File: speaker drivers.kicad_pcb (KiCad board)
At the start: 2 copper layers, 82 x 36.9 mm, 43 parts, among them CN2 10uFE, CN3 0.1uFC

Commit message: WIP: Preliminary commit before splitting boards
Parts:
- removed CG2: 10uFE, LBHB:capacitor-D_4mm-L_2.4mm
- removed Cvr1: 0.33uF, LBHB:capacitor-2.5x5mm-L_2.5mm
- removed Cvr2: 0.1uF, LBHB:capacitor-2.5x5mm-L_2.5mm
- removed RS1: 100k, LBHB:resistor-6x2.3mm
- removed SER1: 8P_miniDIN, LBHB:mini-DIN-8-pin
- removed SIGIN1, SIGOUT1: 4P_miniDIN, LBHB:mini-DIN-4-pin
- removed VCTL1: PGA2310, LBHB:DIP-16
- removed VREG1: 78L05, LBHB:TO-92-bent
- added BNCLin1: BNC, Socket_Strips:Socket_Strip_Straight_1x02, F.Cu at (96.2, 92.6)
- added BNCRin1: BNC, Socket_Strips:Socket_Strip_Straight_1x02, F.Cu at (96.2, 59.1)
- added JL1: JUMPER, Socket_Strips:Socket_Strip_Straight_1x02, F.Cu at (84.3, 100.2)
- added JL2: JUMPER3, Socket_Strips:Socket_Strip_Straight_1x03, F.Cu at (96.2, 100.2)
- added JR1: JUMPER, Socket_Strips:Socket_Strip_Straight_1x02, F.Cu at (84.6, 52.7)
- added JR2: JUMPER3, Socket_Strips:Socket_Strip_Straight_1x03, F.Cu at (96.2, 52.7)
- added Lout1: CONN_01X02, Socket_Strips:Socket_Strip_Straight_1x02, F.Cu at (66.5, 103.9)
- added Rout1: CONN_01X02, Socket_Strips:Socket_Strip_Straight_1x02, F.Cu at (66.8, 72.3)
- BUFL1, BUFL2, BUFR1, BUFR2: moved to B.Cu
- PWR1: value 4P_miniDIN_PWR -> CONN_01X03; footprint LBHB:mini-DIN-4-pin -> Socket_Strips:Socket_Strip_Straight_1x03
- moved PWR1 66.8 mm to (97.9, 74.9), turned to 270 degrees
- moved C2 56.1 mm to (78.8, 70.0)
- moved CR1 55.9 mm to (75.6, 57.8)
- moved CR6 55.9 mm to (79.6, 57.9)
- moved RR4 50.9 mm to (65.6, 59.9), turned to 270 degrees
- moved RR3 49.1 mm to (90.9, 60.9), turned to 270 degrees
- moved BUFR1 49.1 mm to (70.5, 60.0), turned to 90 degrees
- moved BUFR2 49.0 mm to (83.7, 60.0), turned to 90 degrees
- moved RL2 46.6 mm to (76.0, 84.2)
- moved CN2 45.5 mm to (90.6, 74.5)
- moved CN3 45.3 mm to (94.6, 74.6)
- moved RR1 44.2 mm to (88.0, 60.9), turned to 90 degrees
- moved CR3 43.4 mm to (60.7, 72.8)
- moved CR2 43.1 mm to (75.6, 64.7), turned to 90 degrees
- moved CR5 43.1 mm to (79.6, 64.7), turned to 270 degrees
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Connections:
- OPA1 pad 1: Net-(BUFL1-Pad2) -> Net-(BUFR1-Pad2)
- OPA1 pad 2: Net-(OPA1-Pad2) -> Net-(JR2-Pad2)
- OPA1 pad 3: Net-(OPA1-Pad3) -> Net-(CRin1-Pad1)
- OPA1 pad 5: Net-(OPA1-Pad5) -> Net-(CLin1-Pad1)
- OPA1 pad 6: Net-(OPA1-Pad6) -> Net-(JL2-Pad2)
- OPA1 pad 7: Net-(BUFR1-Pad2) -> Net-(BUFL1-Pad2)
- PWR1 pad 1: AGND -> -12V
- RL1 pad 1: Net-(OPA1-Pad2) -> Net-(JL2-Pad2)
- RL1 pad 2: AGND -> Net-(JL1-Pad2)
- RL2 pad 2: Net-(OPA1-Pad2) -> Net-(JL2-Pad2)
- RL3 pad 2: Net-(OPA1-Pad3) -> Net-(CLin1-Pad1)
- RR1 pad 1: Net-(OPA1-Pad6) -> Net-(JR2-Pad2)
- RR1 pad 2: AGND -> Net-(JR1-Pad2)
- RR2 pad 2: Net-(OPA1-Pad6) -> Net-(JR2-Pad2)
- RR3 pad 2: Net-(OPA1-Pad5) -> Net-(CRin1-Pad1)
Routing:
- net +12V: track 183.2 -> 39.1 mm
- net -12V: track 137.3 -> 64.3 mm, vias 3 -> 0
- net /MUTE: track 46.6 -> 0.00 mm
- net Net-(BNCRin1-Pad1): track 49.9 -> 6.60 mm
- net Net-(SIGIN1-Pad2): track 34.3 -> 0.00 mm
- net /SCLK: track 31.8 -> 0.00 mm
- net Net-(OPA1-Pad3): track 19.8 -> 0.00 mm
- net Net-(OPA1-Pad2): track 18.3 -> 0.00 mm
- net Net-(BUFR1-Pad4): track 22.5 -> 39.6 mm
- net Net-(CG2-Pad1): track 16.2 -> 0.00 mm
- net Net-(CR3-Pad2): track 29.6 -> 13.6 mm
- net Net-(JR2-Pad2): track 0.00 -> 15.3 mm
- net Net-(JL2-Pad2): track 0.00 -> 15.2 mm
- net Net-(OPA1-Pad5): track 14.3 -> 0.00 mm
- net Net-(BUFR1-Pad2): track 27.0 -> 13.2 mm
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- added copper zone on F.Cu, net AGND
- removed copper zone on B.Cu, net AGND
- removed copper zone on B.Cu, net DGND
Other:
- board outline removed
- board text removed: "Speaker Driver V2 Design by BNB (OHSU LBHB) bburan@alum.mit.edu 2015.02.20"

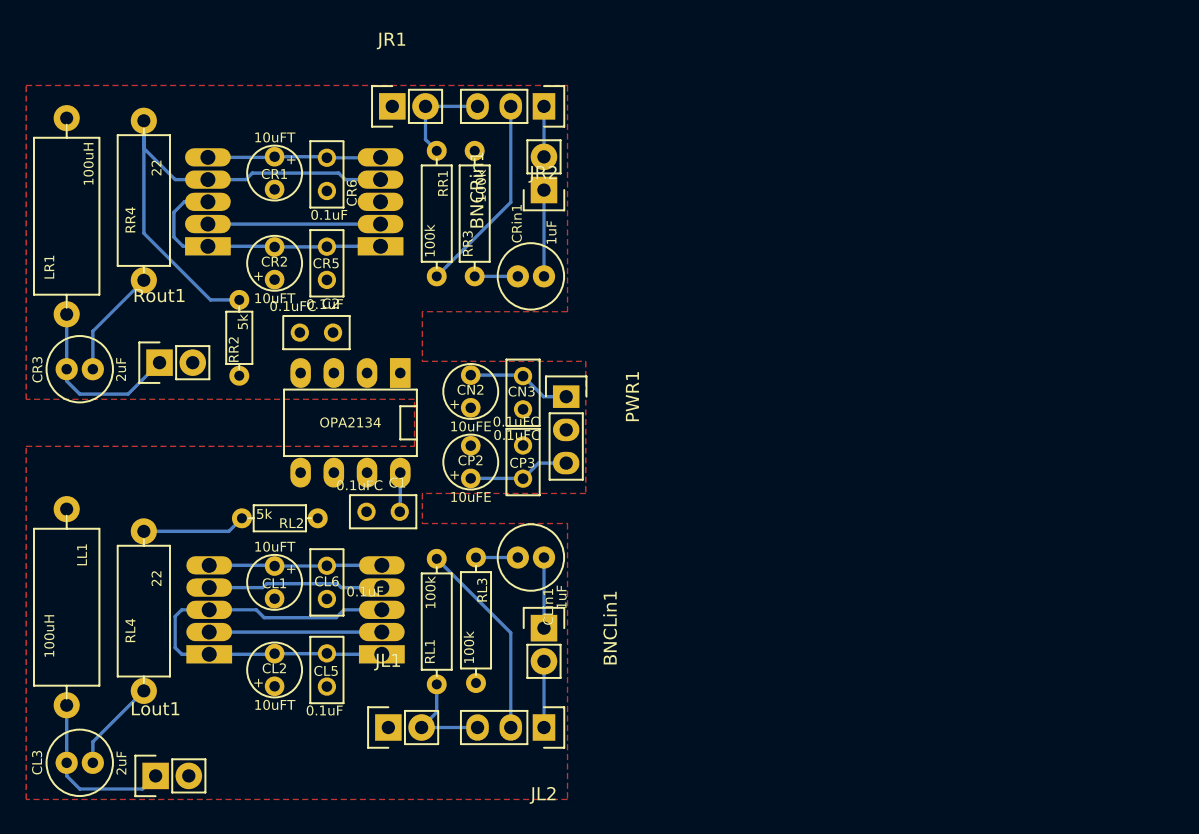
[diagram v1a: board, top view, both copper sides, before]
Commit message: WIP: Test of new circuit for speaker drivers
Note that this circuit does not work and should not be used for
production.
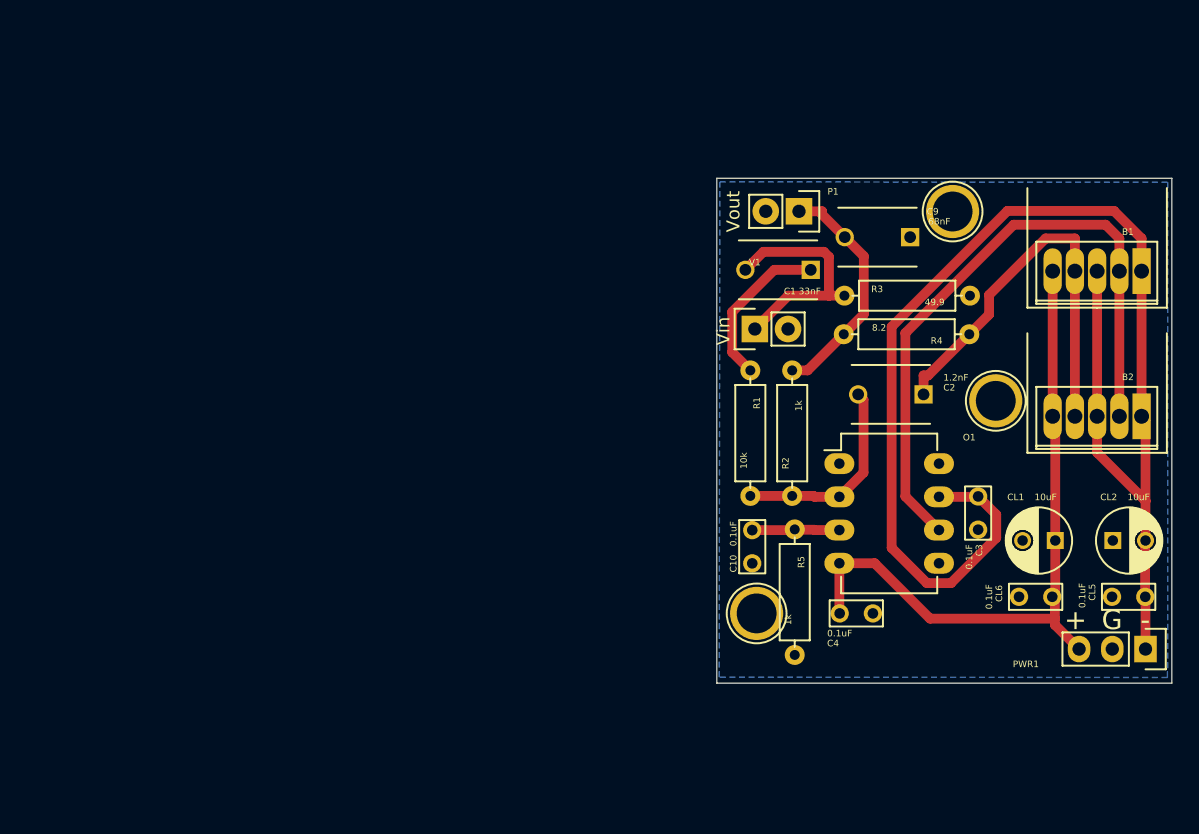
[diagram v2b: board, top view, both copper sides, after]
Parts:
- removed BNCLin1, BNCRin1: BNC, Socket_Strips:Socket_Strip_Straight_1x02
- removed BUFL1, BUFL2, BUFR1, BUFR2: BUF634, LBHB:BUF634
- removed CL3, CR3: 2uF, LBHB:capacitor-D_5mm-L_2mm
- removed CLin1, CRin1: 1uF, LBHB:capacitor-D_5mm-L_2mm
- removed CN2, CP2: 10uFE, LBHB:capacitor-D_4mm-L_2.4mm
- removed CN3, CP3: 0.1uFC, LBHB:capacitor-2.5x5mm-L_2.5mm
- removed CR1, CR2: 10uFT, LBHB:capacitor-D_4mm-L_2.4mm
- removed CR5, CR6: 0.1uF, LBHB:capacitor-2.5x5mm-L_2.5mm
- removed JL1, JR1: JUMPER, Socket_Strips:Socket_Strip_Straight_1x02
- removed JL2, JR2: JUMPER3, Socket_Strips:Socket_Strip_Straight_1x03
- removed LL1, LR1: 100uH, LBHB:inductor-12mm
- removed Lout1, Rout1: CONN_01X02, Socket_Strips:Socket_Strip_Straight_1x02
- removed OPA1: OPA2134, LBHB:DIP-8
- removed RL1, RL3, RR1, RR3: 100k, LBHB:resistor-6x2.3mm
- removed RL2, RR2: 5k, LBHB:resistor-4x2mm
- removed RL4, RR4: 22, LBHB:resistor-13x4mm
- added B1: BUF634, LBHB:BUF634_compact_HeatSink, F.Cu at (138.5, 65.3)
- added B2: BUF634, LBHB:BUF634_compact_HeatSink, F.Cu at (138.5, 76.4)
- added C10: 0.1uF, LBHB:capacitor-2x4mm-L_2.5mm, F.Cu at (112.1, 86.4)
- added C3: 0.1uF, LBHB:capacitor-2x4mm-L_2.5mm, F.Cu at (129.4, 83.8)
- added C4: 0.1uF, LBHB:capacitor-2x4mm-L_2.5mm, F.Cu at (120.0, 91.5)
- added C9: 68nF, Capacitors_ThroughHole:C_Disc_D6_P5, F.Cu at (124.2, 62.7)
- added O1: OPA134, Housings_DIP:DIP-8_W7.62mm_LongPads, F.Cu at (118.7, 80.0)
- added P1: CONN_01X02, Socket_Strips:Socket_Strip_Straight_1x02, F.Cu at (115.7, 60.7)
- added R1: 10k, LBHB:resistor-6x2.3mm, F.Cu at (111.9, 77.7)
- added R2: 1k, LBHB:resistor-6x2.3mm, F.Cu at (115.1, 77.7)
- added R3: 49.9, LBHB:resistor-6x2.3mm, F.Cu at (123.9, 67.2)
- added R4: 8.2, LBHB:resistor-6x2.3mm, F.Cu at (123.9, 70.1)
- added R5: 1k, LBHB:resistor-6x2.3mm, F.Cu at (115.3, 89.8)
- added REF**: 1pin, Connect:1pin, F.Cu at (127.4, 60.7)
- added REF**: 1pin, Connect:1pin, F.Cu at (130.7, 75.2)
- added REF**: 1pin, Connect:1pin, F.Cu at (112.4, 91.5)
- added V1: BNC, Socket_Strips:Socket_Strip_Straight_1x02, F.Cu at (112.3, 69.7)
- C1: value 0.1uFC -> 33nF; footprint LBHB:capacitor-2.5x5mm-L_2.5mm -> Capacitors_ThroughHole:C_Disc_D6_P5
- C2: value 0.1uFC -> 1.2nF; footprint LBHB:capacitor-2.5x5mm-L_2.5mm -> Capacitors_ThroughHole:C_Disc_D6_P5
- CL1, CL2: value 10uFT -> 10uF; footprint LBHB:capacitor-D_4mm-L_2.4mm -> Capacitors_ThroughHole:C_Radial_D5_L6_P2.5
- CL5, CL6: footprint LBHB:capacitor-2.5x5mm-L_2.5mm -> LBHB:capacitor-2x4mm-L_2.5mm
- moved CL2 64.9 mm to (139.7, 85.9), turned to 0 degrees
- moved CL5 61.6 mm to (140.9, 90.2), turned to 180 degrees
- moved CL1 59.8 mm to (135.3, 85.9), turned to 180 degrees
- moved CL6 54.2 mm to (133.8, 90.2), turned to 180 degrees
- moved PWR1 48.3 mm to (142.2, 94.2), turned to 180 degrees
- moved C2 46.7 mm to (125.2, 74.7), turned to 180 degrees
- moved C1 37.6 mm to (116.6, 65.2), turned to 180 degrees
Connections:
- C1 pad 1: AGND -> Net-(C1-Pad1)
- C1 pad 2: +12V -> Net-(C1-Pad2)
- C2 pad 1: -12V -> Net-(B1-Pad4)
- C2 pad 2: AGND -> Net-(C2-Pad2)
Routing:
- net Net-(B1-Pad2): track 0.00 -> 50.0 mm
- net -12V: track 64.3 -> 108.5 mm
- net Net-(BUFR1-Pad4): track 39.6 -> 0.00 mm
- net Net-(B1-Pad4): track 0.00 -> 31.8 mm
- net Net-(BUFL1-Pad4): track 21.4 -> 0.00 mm
- net Net-(C9-Pad2): track 0.00 -> 18.2 mm
- net Net-(C1-Pad2): track 0.00 -> 18.0 mm
- net Net-(C2-Pad2): track 0.00 -> 15.6 mm
- net Net-(JR2-Pad2): track 15.3 -> 0.00 mm
- net Net-(JL2-Pad2): track 15.2 -> 0.00 mm
- net Net-(CR3-Pad2): track 13.6 -> 0.00 mm
- net Net-(BUFR1-Pad2): track 13.2 -> 0.00 mm
- net Net-(BUFL1-Pad2): track 13.2 -> 0.00 mm
- net Net-(CL3-Pad2): track 13.0 -> 0.00 mm
- net +12V: track 39.1 -> 51.8 mm
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- added copper zone on B.Cu, net AGND
- removed copper zone on F.Cu, net AGND
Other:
- board outline added: 34.8 x 38.6 mm
- net class Default: clearance 0.254 -> 0.3; trace_width 0.254 -> 0.75
- net class High current signal removed
- net class Power: clearance 0.254 -> 0.3; trace_width 0.254 -> 0.75
- rule trace_clearance: 0.254 -> 0.3
- board text added: "+"
- board text added: "-"
- board text added: "G"
- board text added: "Vin"
- board text added: "Vout"

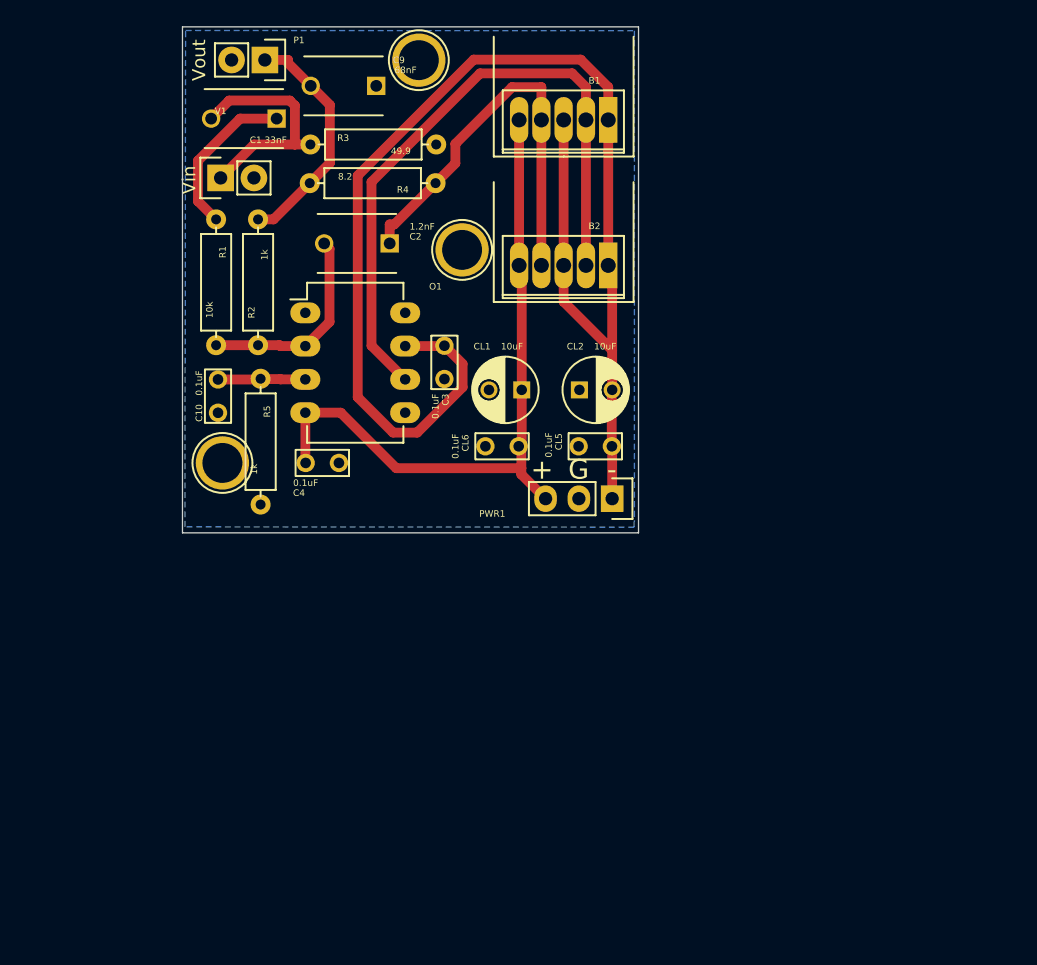
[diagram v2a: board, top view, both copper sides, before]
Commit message: ENH: Revisions to speaker drivers
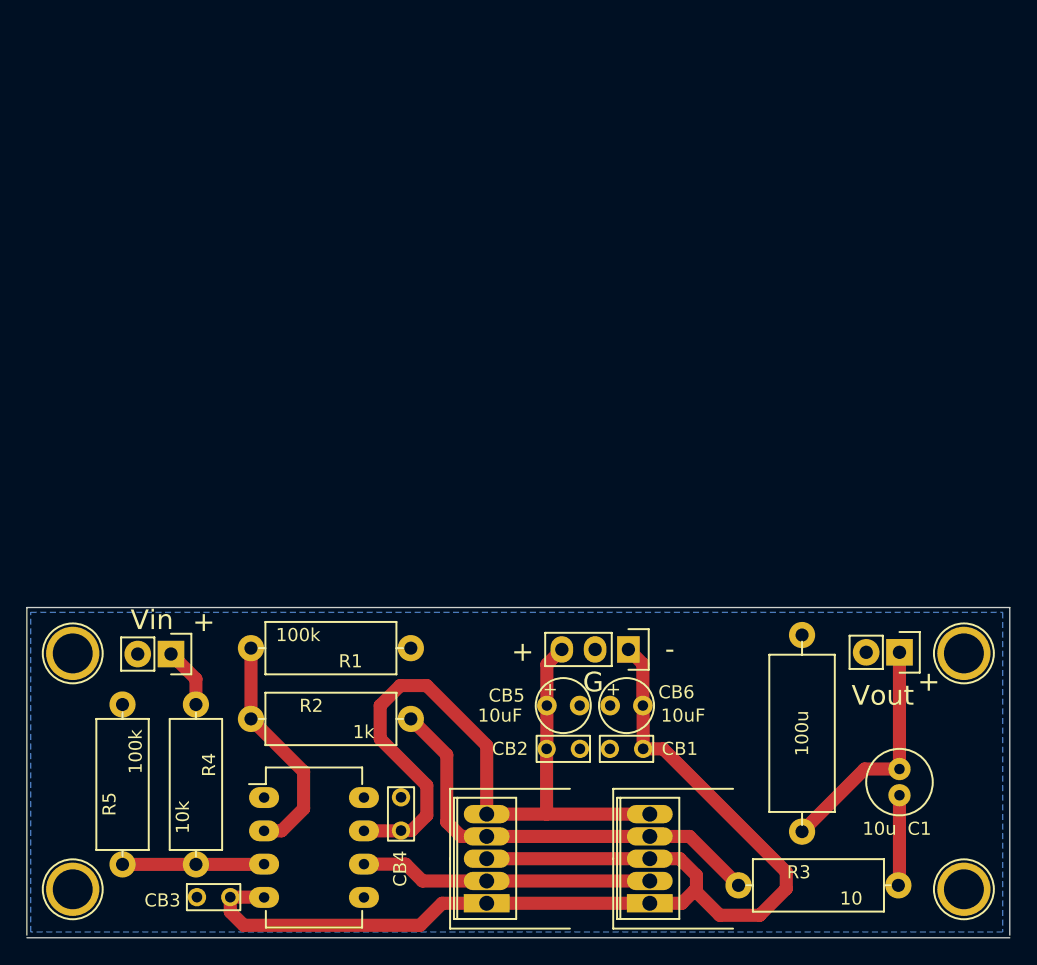
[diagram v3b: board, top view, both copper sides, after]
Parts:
- removed C10, C3, C4, CL5, CL6: 0.1uF, LBHB:capacitor-2x4mm-L_2.5mm
- removed C2: 1.2nF, Capacitors_ThroughHole:C_Disc_D6_P5
- removed C9: 68nF, Capacitors_ThroughHole:C_Disc_D6_P5
- removed CL1, CL2: 10uF, Capacitors_ThroughHole:C_Radial_D5_L6_P2.5
- removed the REF** at (127.4, 60.7)
- removed the REF** at (130.7, 75.2)
- removed the REF** at (112.4, 91.5)
- added CB1: 0.1uF, LBHB:capacitor-2x4mm-L_2.5mm, F.Cu at (143.3, 113.3)
- added CB2: 0.1uF, LBHB:capacitor-2x4mm-L_2.5mm, F.Cu at (138.4, 113.3)
- added CB3: 0.1uF, LBHB:capacitor-2x4mm-L_2.5mm, F.Cu at (111.8, 124.6)
- added CB4: 0.1uF, LBHB:capacitor-2x4mm-L_2.5mm, F.Cu at (126.0, 118.2)
- added CB5: 10uF, LBHB:capacitor-D_4mm-L_2.4mm, F.Cu at (138.4, 110.0)
- added CB6: 10uF, LBHB:capacitor-D_4mm-L_2.4mm, F.Cu at (143.3, 110.0)
- added L1: 100u, LBHB:inductor-12mm, F.Cu at (158.7, 112.1)
- added REF**: 1pin, Connect:1pin, F.Cu at (101.0, 124.0)
- added REF**: 1pin, Connect:1pin, F.Cu at (169.0, 106.0)
- added REF**: 1pin, Connect:1pin, F.Cu at (101.0, 106.0)
- added REF**: 1pin, Connect:1pin, F.Cu at (169.0, 124.0)
- C1: value 33nF -> 10u; footprint Capacitors_ThroughHole:C_Disc_D6_P5 -> LBHB:capacitor-D_5mm-L_2mm
- R1: value 10k -> 100k; footprint LBHB:resistor-6x2.3mm -> LBHB:resistor-13x4mm
- R2: footprint LBHB:resistor-6x2.3mm -> LBHB:resistor-13x4mm
- R3: value 49.9 -> 10; footprint LBHB:resistor-6x2.3mm -> LBHB:resistor-13x4mm
- R4: value 8.2 -> 10k; footprint LBHB:resistor-6x2.3mm -> LBHB:resistor-13x4mm
- R5: value 1k -> 100k; footprint LBHB:resistor-6x2.3mm -> LBHB:resistor-13x4mm
- moved C1 69.4 mm to (164.1, 115.8)
- moved P1 66.2 mm to (164.1, 105.9)
- moved R3 65.9 mm to (157.9, 123.7)
- moved B1 56.8 mm to (145.0, 121.7), turned to 90 degrees
- moved R4 47.8 mm to (110.4, 116.0), turned to 90 degrees
- moved B2 45.7 mm to (132.6, 121.7), turned to 90 degrees
- moved O1 37.1 mm to (115.6, 117.0)
- moved V1 36.5 mm to (108.5, 106.0), turned to 180 degrees
- moved R2 33.8 mm to (120.7, 111.0), turned to 180 degrees
- moved R1 29.3 mm to (120.7, 105.6), turned to 0 degrees
- moved R5 28.2 mm to (104.8, 116.0), turned to 270 degrees
- moved PWR1 11.6 mm to (143.4, 105.7)
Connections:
- O1 pad 3: Net-(C10-Pad2) -> Net-(O1-Pad3)
- O1 pad 4: +12V -> -12V
- O1 pad 7: -12V -> +12V
- P1 pad 1: Net-(C9-Pad2) -> Net-(C1-Pad1)
- R1 pad 2: Net-(C1-Pad1) -> AGND
- R2 pad 1: Net-(C9-Pad2) -> Net-(B1-Pad4)
- R3 pad 1: AGND -> Net-(C1-Pad2)
- R3 pad 2: Net-(C1-Pad2) -> Net-(B1-Pad4)
- R4 pad 1: Net-(C9-Pad2) -> Net-(O1-Pad3)
- R4 pad 2: Net-(B1-Pad4) -> Net-(R4-Pad2)
- R5 pad 2: Net-(C10-Pad2) -> Net-(O1-Pad3)
- V1 pad 1: Net-(C1-Pad2) -> Net-(R4-Pad2)
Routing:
- net Net-(B1-Pad2): track 50.0 -> 22.3 mm
- net Net-(C9-Pad2): track 18.2 -> 0.00 mm
- net -12V: track 108.5 -> 91.2 mm
- net Net-(C1-Pad2): track 18.0 -> 6.91 mm
- net Net-(O1-Pad3): track 0.00 -> 10.8 mm
- net Net-(C10-Pad2): track 6.71 -> 0.00 mm
- net Net-(C1-Pad1): track 12.4 -> 18.4 mm
- net +12V: track 51.8 -> 56.5 mm
- net Net-(R4-Pad2): track 0.00 -> 4.64 mm
- net Net-(O1-Pad2): track 15.6 -> 17.6 mm
- net Net-(B1-Pad4): track 31.8 -> 33.3 mm
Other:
- board size 34.8 x 38.6 mm -> 75 x 25.2 mm
- net class Default: clearance 0.3 -> 0.4; trace_width 0.75 -> 1; via_dia 0.889 -> 0.6; via_drill 0.635 -> 0.4
- net class Power removed
- rule trace_clearance: 0.3 -> 0.4
- rule trace_min: 0.254 -> 0.2
- rule via_min_drill: 0.508 -> 0.3
- rule via_min_size: 0.889 -> 0.4
